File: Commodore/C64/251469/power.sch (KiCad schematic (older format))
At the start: 17 parts, among them CN10 LED Connector, CN7 Power Input, SW1 Power Switch

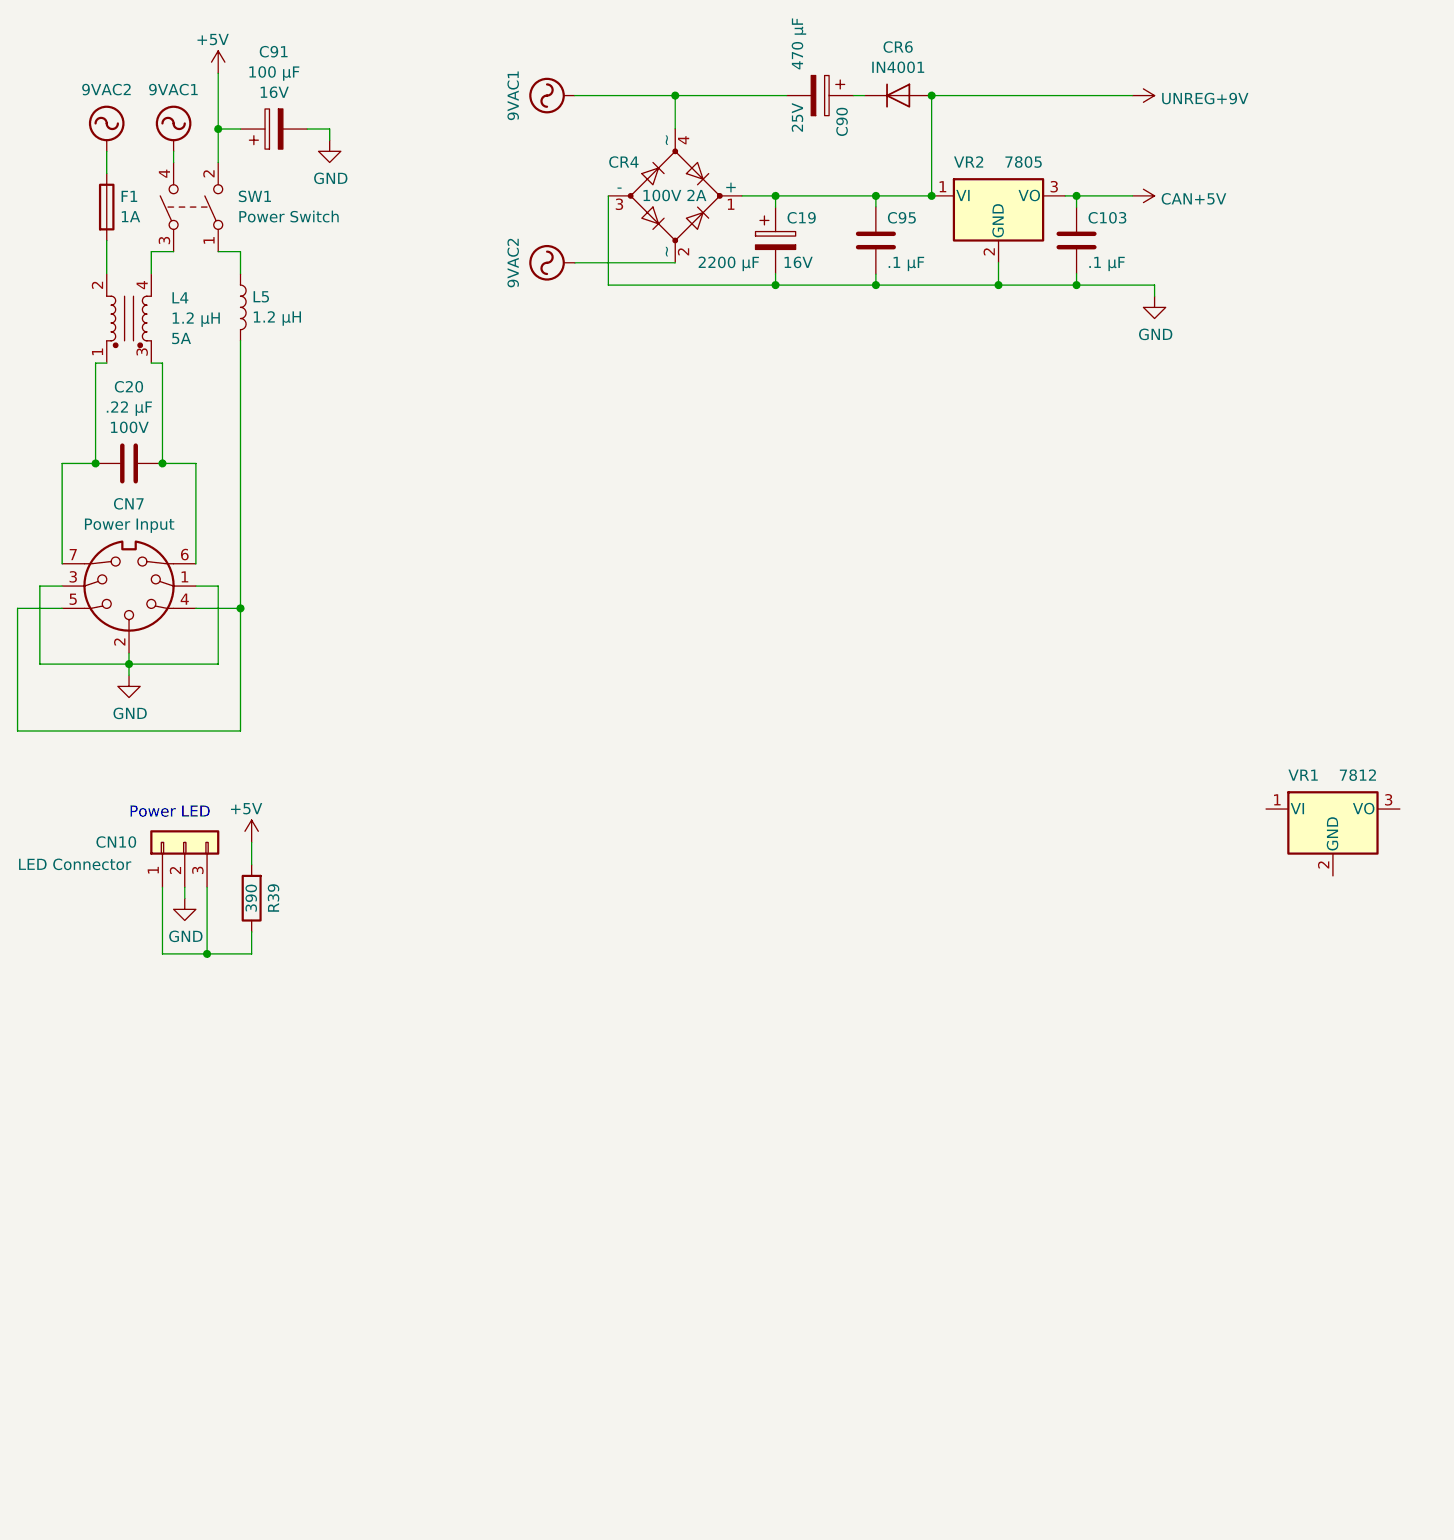
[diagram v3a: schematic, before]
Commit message: +12V regulation circuit added
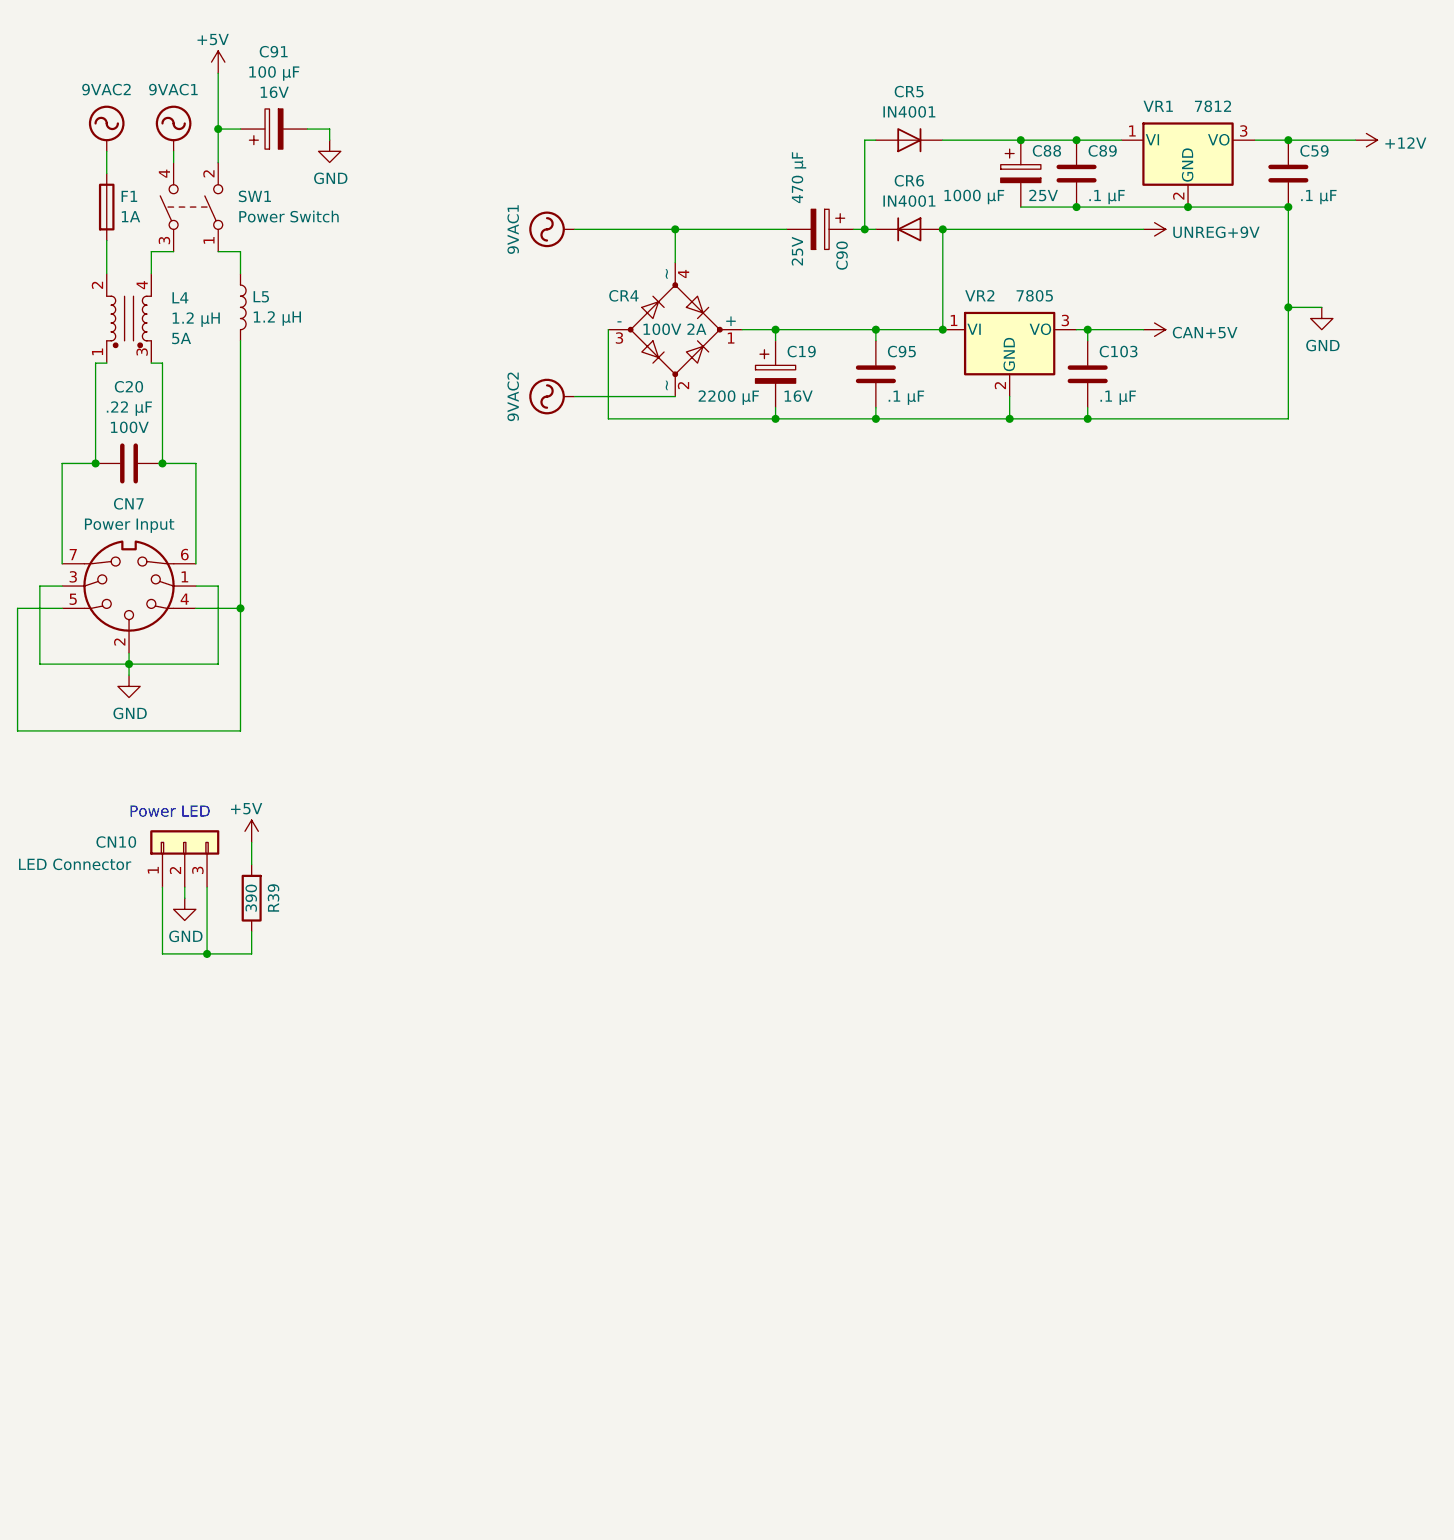
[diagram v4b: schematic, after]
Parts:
- added C59, C89: .1 μF, symbol Device:C
- added C88: 1000 μF, symbol Device:CP
- added CR5: IN4001, symbol Device:D
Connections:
- net GND: now also VR1.2 (GND), C59.2, C88.2, C89.2
- net at C90.1, CR6.1 (K): now also CR5.2 (A)
- net at VR1.1 (VI): now also C88.1, C89.1, CR5.1 (K)
- net +12V: now reaches VR1.3 (VO)
- net +12V: now also C59.1
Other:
- moved on the sheet: C103, C19, C90, C95, CR4, CR6, VR1, VR2

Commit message: Tweaks
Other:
- moved on the sheet: C103, C19, C59, C88, C89, C90, C95, CR4, CR5, CR6, VR1, VR2

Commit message: WIP
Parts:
- added C22, C31: .1 μF, symbol Device:C_Small
- added U15: 74LS139, symbol 74xx:74LS139
- added U8: 7406, symbol 74xx_more:7406
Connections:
- net +5V: now also C22.2, C31.2, U15.16 (VCC), U8.14 (VCC)
- net GND: now also C22.1, C31.1, U15.8 (GND), U8.7 (GND)
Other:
- moved on the sheet: CN10, R39
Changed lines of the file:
@@
 L Connector_Generic:Conn_01x03 CN10
 U 1 1 5D326E0E
-P 1350 4200
-F 0 "CN10" V 1350 4600 50  0000 R CNN
-F 1 "LED Connector" V 1250 4950 50  0000 R CNN
-F 2 "" H 1350 4200 50  0001 C CNN
-F 3 "~" H 1350 4200 50  0001 C CNN
-	1    1350 4200
+P 2750 2850
+F 0 "CN10" V 2750 3250 50  0000 R CNN
+F 1 "LED Connector" V 2650 3600 50  0000 R CNN
+F 2 "" H 2750 2850 50  0001 C CNN
+F 3 "~" H 2750 2850 50  0001 C CNN
+	1    2750 2850
 	0    -1   -1   0
 $EndComp
@@
 L power:+5V #PWR?
 U 1 1 5D329DED
-P 1650 4200
+P 3050 2850
 AR Path="/5D329DED" Ref="#PWR?"  Part="1"
 AR Path="/5D28EBAC/5D329DED" Ref="#PWR?"  Part="1"
 AR Path="/5D4AE438/5D329DED" Ref="#PWR?"  Part="1"
 AR Path="/5D94F152/5D329DED" Ref="#PWR?"  Part="1"
-F 0 "#PWR?" H 1650 4050 50  0001 C CNN
-F 1 "+5V" H 1550 4350 50  0000 L CNN
-F 2 "" H 1650 4200 50  0001 C CNN
-F 3 "" H 1650 4200 50  0001 C CNN
-	1    1650 4200
-	1    0    0    -1
-$EndComp
-Wire Wire Line
-	1650 4300 1650 4200
+F 0 "#PWR?" H 3050 2700 50  0001 C CNN
+F 1 "+5V" H 2950 3000 50  0000 L CNN
+F 2 "" H 3050 2850 50  0001 C CNN
+F 3 "" H 3050 2850 50  0001 C CNN
+	1    3050 2850
+	1    0    0    -1
+$EndComp
+Wire Wire Line
+	3050 2950 3050 2850
 $Comp
 L power:GND #PWR?
 U 1 1 5D32A5A8
-P 1350 4450
+P 2750 3100
 AR Path="/5D32A5A8" Ref="#PWR?"  Part="1"
 AR Path="/5D94F152/5D32A5A8" Ref="#PWR?"  Part="1"
-F 0 "#PWR?" H 1350 4200 50  0001 C CNN
-F 1 "GND" H 1355 4277 50  0000 C CNN
-F 2 "" H 1350 4450 50  0001 C CNN
-F 3 "" H 1350 4450 50  0001 C CNN
-	1    1350 4450
-	1    0    0    -1
-$EndComp
-Wire Wire Line
-	1350 4450 1350 4400
-Wire Wire Line
-	1250 4400 1250 4700
-Wire Wire Line
-	1250 4700 1450 4700
-Wire Wire Line
-	1450 4700 1450 4400
+F 0 "#PWR?" H 2750 2850 50  0001 C CNN
+F 1 "GND" H 2755 2927 50  0000 C CNN
+F 2 "" H 2750 3100 50  0001 C CNN
+F 3 "" H 2750 3100 50  0001 C CNN
+	1    2750 3100
+	1    0    0    -1
+$EndComp
+Wire Wire Line
+	2750 3100 2750 3050
+Wire Wire Line
+	2650 3050 2650 3350
+Wire Wire Line
+	2650 3350 2850 3350
+Wire Wire Line
+	2850 3350 2850 3050
 $Comp
 L Device:R R39
 U 1 1 5D327CB8
-P 1650 4450
-F 0 "R39" V 1550 4450 50  0000 C CNN
-F 1 "390" V 1650 4450 50  0000 C CNN
-F 2 "" V 1580 4450 50  0001 C CNN
-F 3 "~" H 1650 4450 50  0001 C CNN
-	1    1650 4450
+P 3050 3100
+F 0 "R39" V 2950 3100 50  0000 C CNN
+F 1 "390" V 3050 3100 50  0000 C CNN
+F 2 "" V 2980 3100 50  0001 C CNN
+F 3 "~" H 3050 3100 50  0001 C CNN
+	1    3050 3100
 	-1   0    0    1
 $EndComp
 Wire Wire Line
-	1450 4700 1650 4700
-Wire Wire Line
-	1650 4700 1650 4600
-Connection ~ 1450 4700
-Text Notes 1100 4100 0    50   ~ 0
+	2850 3350 3050 3350
+Wire Wire Line
+	3050 3350 3050 3250
+Connection ~ 2850 3350
+Text Notes 2500 2750 0    50   ~ 0
 Power LED
 $Comp
@@
 	1    0    0    -1
 $EndComp
+$Comp
+L 74xx:74LS139 U?
+U 3 1 5D32511D
+P 4950 3450
+AR Path="/5D4AE438/5D32511D" Ref="U?"  Part="3"
+AR Path="/5D94F152/5D32511D" Ref="U15"  Part="3"
+F 0 "U15" H 4650 3800 50  0000 L CNN
+F 1 "74LS139" H 5000 3800 50  0000 L CNN
+F 2 "" H 4950 3450 50  0001 C CNN
+F 3 "http://www.ti.com/lit/gpn/sn74LS139" H 4950 3450 50  0001 C CNN
+	3    4950 3450
+	1    0    0    -1
+$EndComp
+Wire Wire Line
+	5250 2750 5250 2800
+Wire Wire Line
+	5200 2750 5250 2750
+Wire Wire Line
+	4950 2750 5000 2750
+$Comp
+L power:GND #PWR?
+U 1 1 5D325127
+P 5250 2800
+AR Path="/5D325127" Ref="#PWR?"  Part="1"
+AR Path="/5D28EBAC/5D325127" Ref="#PWR?"  Part="1"
+AR Path="/5D4AE438/5D325127" Ref="#PWR?"  Part="1"
+AR Path="/5D94F152/5D325127" Ref="#PWR?"  Part="1"
+F 0 "#PWR?" H 5250 2550 50  0001 C CNN
+F 1 "GND" H 5255 2627 50  0001 C CNN
+F 2 "" H 5250 2800 50  0001 C CNN
+F 3 "" H 5250 2800 50  0001 C CNN
+	1    5250 2800
+	1    0    0    -1
+$EndComp
+$Comp
+L Device:C_Small C?
+U 1 1 5D32512D
+P 5100 2750
+AR Path="/5D32512D" Ref="C?"  Part="1"
+AR Path="/5D28EBAC/5D32512D" Ref="C?"  Part="1"
+AR Path="/5D4AE438/5D32512D" Ref="C?"  Part="1"
+AR Path="/5D94F152/5D32512D" Ref="C31"  Part="1"
+F 0 "C31" V 5000 2700 50  0000 L CNN
+F 1 ".1 μF" V 5200 2600 50  0000 L CNN
+F 2 "" H 5100 2750 50  0001 C CNN
+F 3 "~" H 5100 2750 50  0001 C CNN
+	1    5100 2750
+	0    1    1    0
+$EndComp
+Wire Wire Line
+	4950 2950 4950 2750
+Connection ~ 4950 2750
+$Comp
+L power:GND #PWR?
+U 1 1 5D325135
+P 4950 4000
+AR Path="/5D325135" Ref="#PWR?"  Part="1"
+AR Path="/5D28EBAC/5D325135" Ref="#PWR?"  Part="1"
+AR Path="/5D4AE438/5D325135" Ref="#PWR?"  Part="1"
+AR Path="/5D94F152/5D325135" Ref="#PWR?"  Part="1"
+F 0 "#PWR?" H 4950 3750 50  0001 C CNN
+F 1 "GND" H 4955 3827 50  0001 C CNN
+F 2 "" H 4950 4000 50  0001 C CNN
+F 3 "" H 4950 4000 50  0001 C CNN
+	1    4950 4000
+	1    0    0    -1
+$EndComp
+Wire Wire Line
+	4950 4000 4950 3950
+Connection ~ 4050 2750
+Wire Wire Line
+	4050 2950 4050 2750
+$Comp
+L Device:C_Small C?
+U 1 1 5D32513E
+P 4200 2750
+AR Path="/5D32513E" Ref="C?"  Part="1"
+AR Path="/5D28EBAC/5D32513E" Ref="C?"  Part="1"
+AR Path="/5D4AE438/5D32513E" Ref="C?"  Part="1"
+AR Path="/5D94F152/5D32513E" Ref="C22"  Part="1"
+F 0 "C22" V 4100 2700 50  0000 L CNN
+F 1 ".1 μF" V 4300 2600 50  0000 L CNN
+F 2 "" H 4200 2750 50  0001 C CNN
+F 3 "~" H 4200 2750 50  0001 C CNN
+	1    4200 2750
+	0    1    1    0
+$EndComp
+$Comp
+L power:GND #PWR?
+U 1 1 5D325144
+P 4350 2800
+AR Path="/5D325144" Ref="#PWR?"  Part="1"
+AR Path="/5D28EBAC/5D325144" Ref="#PWR?"  Part="1"
+AR Path="/5D4AE438/5D325144" Ref="#PWR?"  Part="1"
+AR Path="/5D94F152/5D325144" Ref="#PWR?"  Part="1"
+F 0 "#PWR?" H 4350 2550 50  0001 C CNN
+F 1 "GND" H 4355 2627 50  0001 C CNN
+F 2 "" H 4350 2800 50  0001 C CNN
+F 3 "" H 4350 2800 50  0001 C CNN
+	1    4350 2800
+	1    0    0    -1
+$EndComp
+Wire Wire Line
+	4050 2750 4100 2750
+Wire Wire Line
+	4300 2750 4350 2750
+Wire Wire Line
+	4350 2750 4350 2800
+Wire Wire Line
+	4050 4000 4050 3950
+$Comp
+L power:GND #PWR?
+U 1 1 5D32514F
+P 4050 4000
+AR Path="/5D32514F" Ref="#PWR?"  Part="1"
+AR Path="/5D28EBAC/5D32514F" Ref="#PWR?"  Part="1"
+AR Path="/5D4AE438/5D32514F" Ref="#PWR?"  Part="1"
+AR Path="/5D94F152/5D32514F" Ref="#PWR?"  Part="1"
+F 0 "#PWR?" H 4050 3750 50  0001 C CNN
+F 1 "GND" H 4055 3827 50  0001 C CNN
+F 2 "" H 4050 4000 50  0001 C CNN
+F 3 "" H 4050 4000 50  0001 C CNN
+	1    4050 4000
+	1    0    0    -1
+$EndComp
+$Comp
+L 74xx_more:7406 U?
+U 7 1 5D325155
+P 4050 3450
+AR Path="/5D4AE438/5D325155" Ref="U?"  Part="7"
+AR Path="/5D94F152/5D325155" Ref="U8"  Part="7"
+F 0 "U8" H 3950 3800 50  0000 R CNN
+F 1 "7406" H 4250 3800 50  0000 R CNN
+F 2 "" H 4050 3450 50  0001 C CNN
+F 3 "https://www.ti.com/lit/ds/symlink/sn7406.pdf" H 4050 3450 50  0001 C CNN
+	7    4050 3450
+	1    0    0    -1
+$EndComp
+$Comp
+L power:+5V #PWR?
+U 1 1 5D32775D
+P 4050 2600
+AR Path="/5D32775D" Ref="#PWR?"  Part="1"
+AR Path="/5D28EBAC/5D32775D" Ref="#PWR?"  Part="1"
+AR Path="/5D4AE438/5D32775D" Ref="#PWR?"  Part="1"
+AR Path="/5D94F152/5D32775D" Ref="#PWR?"  Part="1"
+F 0 "#PWR?" H 4050 2450 50  0001 C CNN
+F 1 "+5V" H 3950 2750 50  0000 L CNN
+F 2 "" H 4050 2600 50  0001 C CNN
+F 3 "" H 4050 2600 50  0001 C CNN
+	1    4050 2600
+	1    0    0    -1
+$EndComp
+$Comp
+L power:+5V #PWR?
+U 1 1 5D327EC5
+P 4950 2600
+AR Path="/5D327EC5" Ref="#PWR?"  Part="1"
+AR Path="/5D28EBAC/5D327EC5" Ref="#PWR?"  Part="1"
+AR Path="/5D4AE438/5D327EC5" Ref="#PWR?"  Part="1"
+AR Path="/5D94F152/5D327EC5" Ref="#PWR?"  Part="1"
+F 0 "#PWR?" H 4950 2450 50  0001 C CNN
+F 1 "+5V" H 4850 2750 50  0000 L CNN
+F 2 "" H 4950 2600 50  0001 C CNN
+F 3 "" H 4950 2600 50  0001 C CNN
+	1    4950 2600
+	1    0    0    -1
+$EndComp
+Wire Wire Line
+	4950 2600 4950 2750
+Wire Wire Line
+	4050 2600 4050 2750
 $EndSCHEMATC
